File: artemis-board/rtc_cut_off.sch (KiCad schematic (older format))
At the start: 15 parts, among them Q1 2N7002, Q10 AO3401A, Q3 2N7002, U7 PCF8563T, U9 TCA6408A, Y2 32.768KHz

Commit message: added comments and swapped polarity of Vin connector
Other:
- note added: "Optional (if fuel gauge is not available)"
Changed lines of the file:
@@
 	-1   0    0    1
 $EndComp
+Text Notes 5100 3950 0    50   ~ 0
+Optional (if fuel gauge is not available)
+Wire Notes Line
+	5050 2450 5050 3950
+Wire Notes Line
+	5300 2200 6600 2200
 $EndSCHEMATC

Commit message: swapped and added some lcsc part numbers and DNP markers
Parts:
- C22: footprint Capacitor_SMD:C_0603_1608Metric_Pad1.05x0.95mm_HandSolder -> Capacitor_SMD:C_0603_1608Metric_Pad1.08x0.95mm_HandSolder
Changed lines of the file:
@@
 F 0 "C22" H 5600 1700 50  0000 L CNN
 F 1 "1µF" H 5600 1900 50  0000 L CNN
-F 2 "Capacitor_SMD:C_0603_1608Metric_Pad1.05x0.95mm_HandSolder" H 5838 1650 50  0001 C CNN
+F 2 "Capacitor_SMD:C_0603_1608Metric_Pad1.08x0.95mm_HandSolder" H 5838 1650 50  0001 C CNN
 F 3 "~" H 5800 1800 50  0001 C CNN
 F 4 "C15849" H 5800 1800 50  0001 C CNN "LCSC"

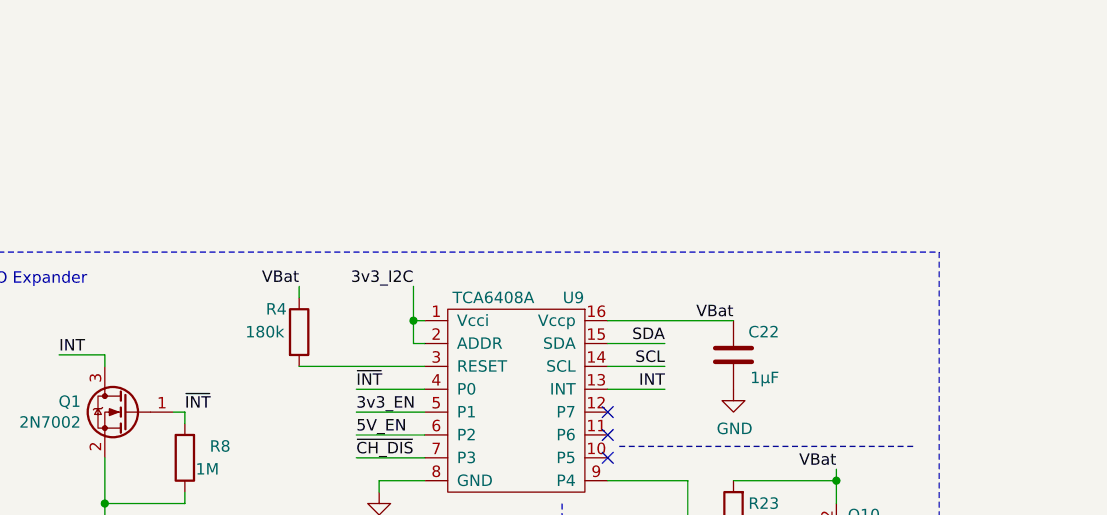
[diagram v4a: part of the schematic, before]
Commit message: added warning comment for expander ic
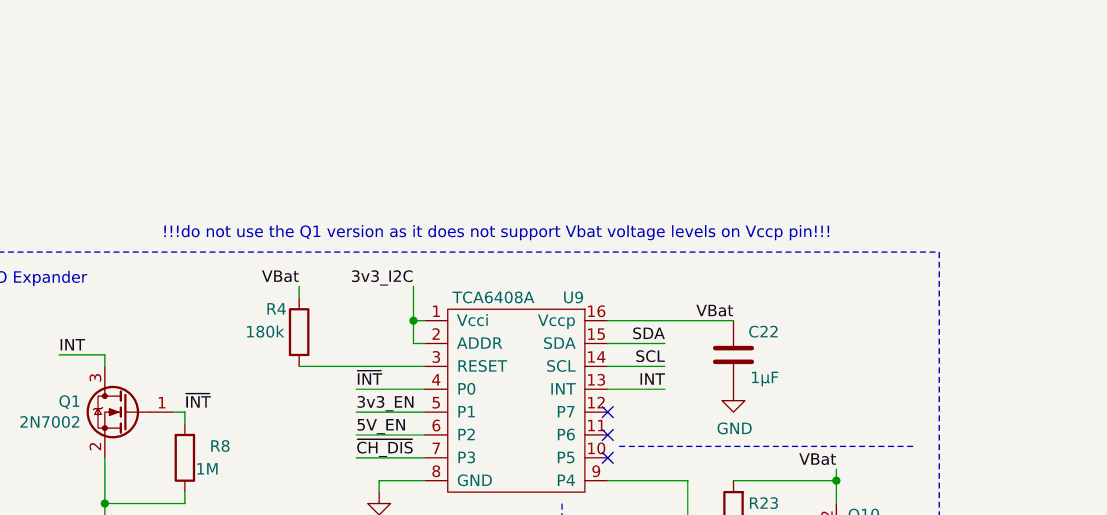
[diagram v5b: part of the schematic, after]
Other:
- note added: "!!!do not use the Q1 version as it does not support Vbat voltage levels on Vccp pin!!!"
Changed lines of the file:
@@
 Wire Notes Line
 	5300 2200 6600 2200
+Text Notes 3300 1300 0    50   ~ 0
+!!!do not use the Q1 version as it does not support Vbat voltage levels on Vccp pin!!!
 $EndSCHEMATC

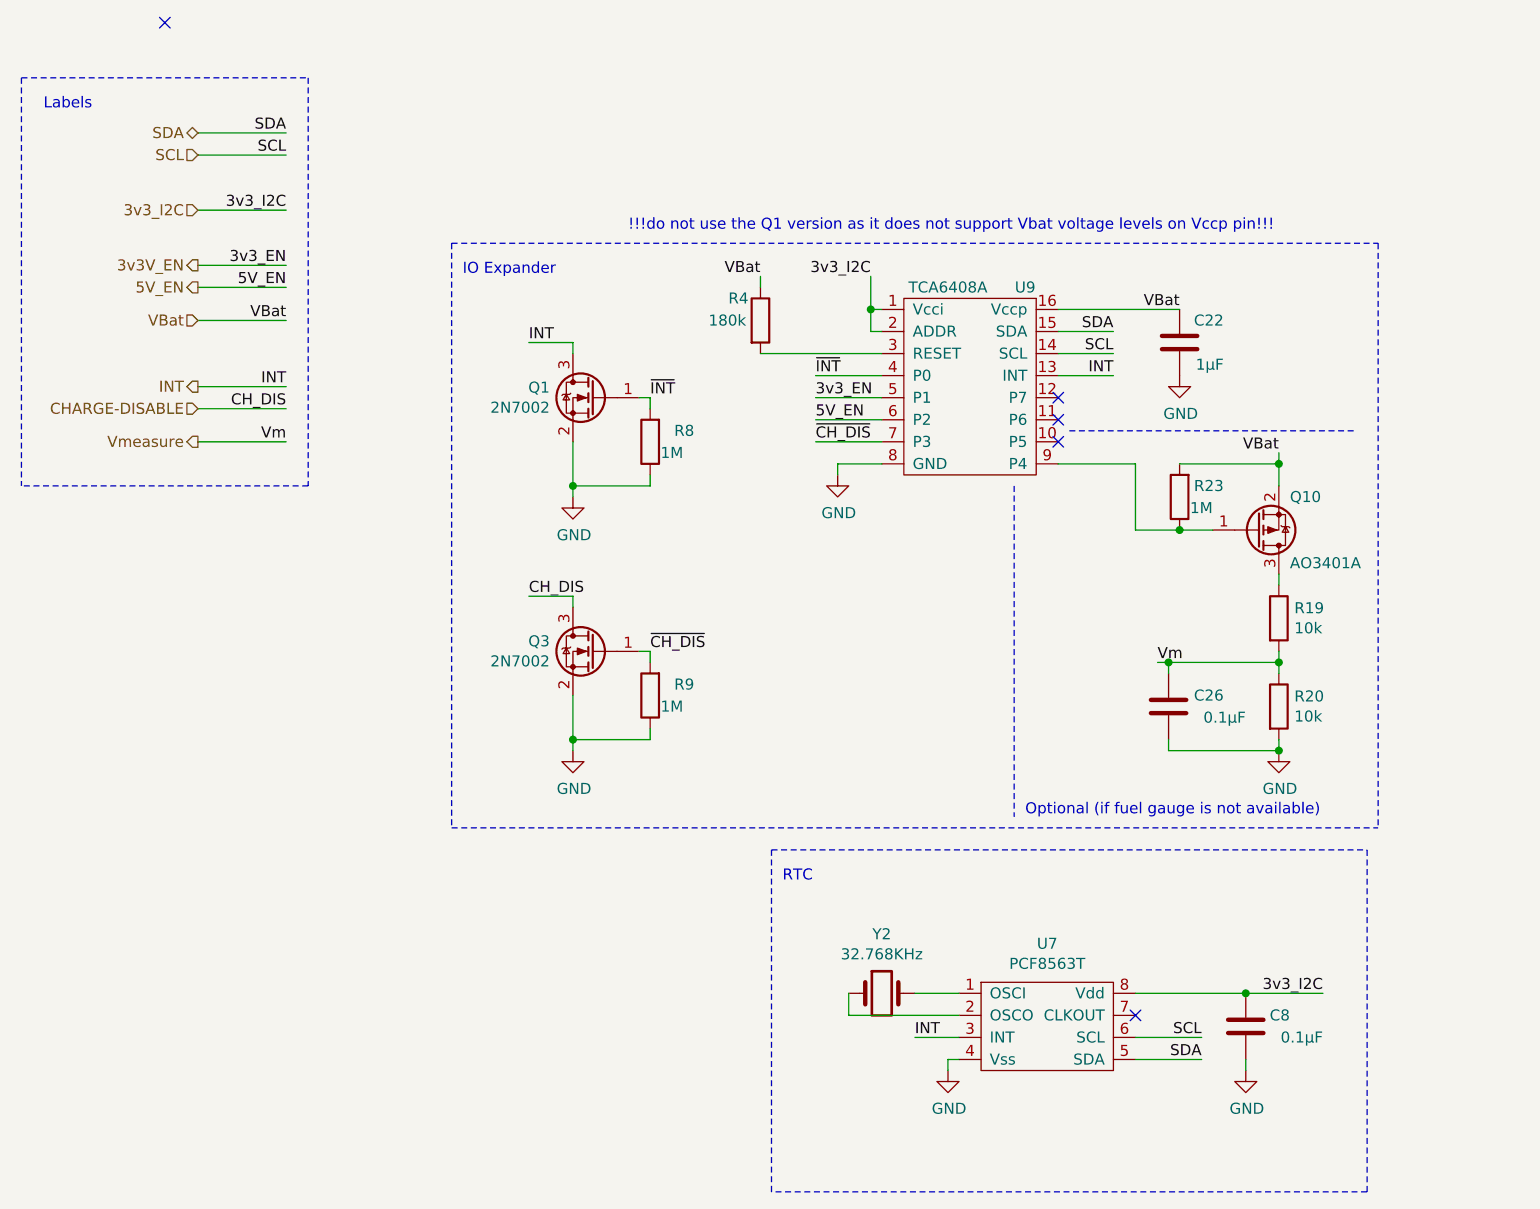
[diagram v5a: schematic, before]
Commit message: connected VccP of io expander back to 3v3, changed some footprint
also added NMos so voltage divider can be used
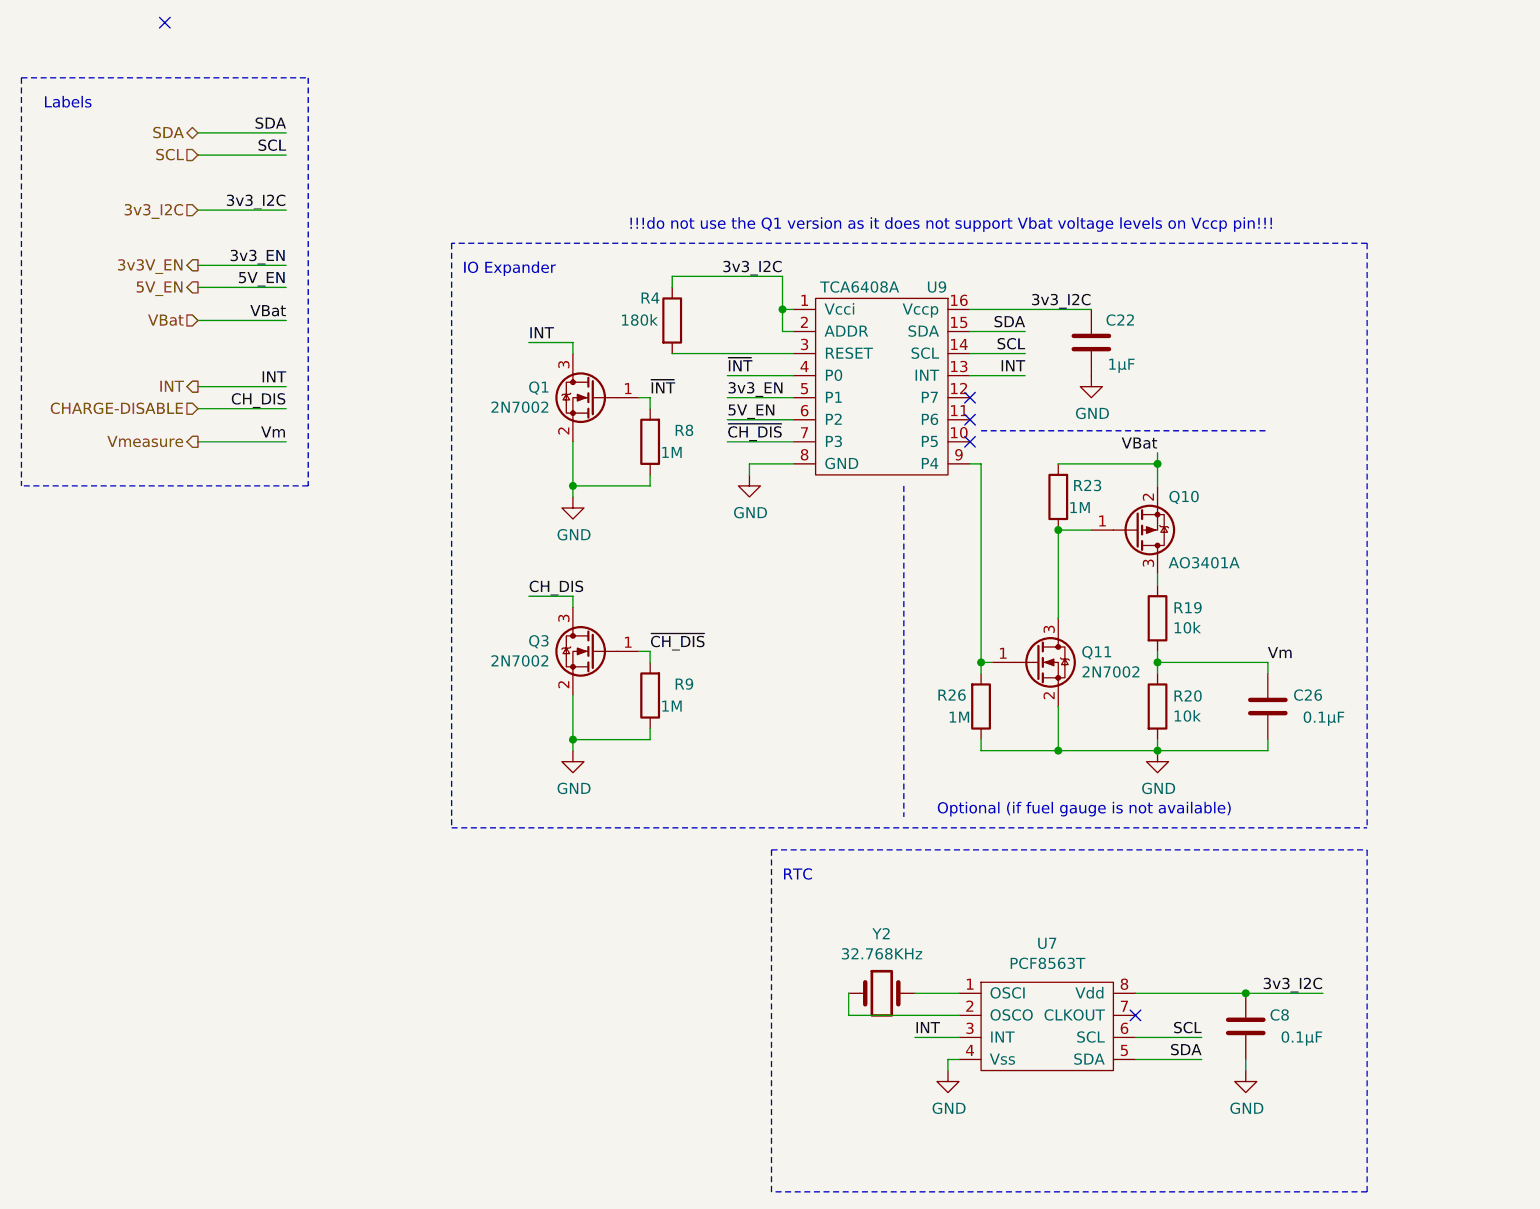
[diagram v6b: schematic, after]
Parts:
- added Q11: 2N7002, Package_TO_SOT_SMD:SOT-23, symbol Transistor_FET:2N7002
- added R26: 1M, Resistor_SMD:R_0603_1608Metric_Pad0.98x0.95mm_HandSolder, symbol Device:R
- Q10: footprint Package_TO_SOT_SMD:SOT-23_Handsoldering -> Package_TO_SOT_SMD:SOT-23
- R23, R8, R9: footprint Resistor_SMD:R_0603_1608Metric_Pad1.05x0.95mm_HandSolder -> Resistor_SMD:R_0603_1608Metric_Pad0.98x0.95mm_HandSolder
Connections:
- net 3v3_I2C: now also C22.2, R4.1, U9.16 (Vccp)
- net GND: now also Q11.2 (S), R26.1
- net VBat: no longer C22.2, R4.1, U9.16 (Vccp)
- net at Q10.1 (G), R23.1: now also Q11.3 (D); no longer U9.9 (P4)
- new net: Q11.1 (G), R26.2, U9.9 (P4)
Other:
- moved on the sheet: C22, C26, Q10, R19, R20, R23, R4, U9

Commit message: added cap to 3v3 I2c, swapped some footprints to normal...
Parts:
- C26, Q10, Q11, R19, R20, R23, R26: DNP (none) -> DNP
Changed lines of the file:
@@
 F 2 "Package_TO_SOT_SMD:SOT-23" H 3350 1975 50  0001 L CIN
 F 3 "https://www.fairchildsemi.com/datasheets/2N/2N7002.pdf" H 3150 2050 50  0001 L CNN
-F 4 "" H 3150 2050 50  0001 C CNN "Field4"
-F 5 "C8545" H 3150 2050 50  0001 C CNN "LCSC"
+F 4 "C8545" H 3150 2050 50  0001 C CNN "LCSC"
 	1    3150 2050
 	-1   0    0    -1
@@
 F 2 "Package_TO_SOT_SMD:SOT-23" H 3350 3125 50  0001 L CIN
 F 3 "https://www.fairchildsemi.com/datasheets/2N/2N7002.pdf" H 3150 3200 50  0001 L CNN
-F 4 "" H 3150 3200 50  0001 C CNN "Field4"
-F 5 "C8545" H 3150 3200 50  0001 C CNN "LCSC"
+F 4 "C8545" H 3150 3200 50  0001 C CNN "LCSC"
 	1    3150 3200
 	-1   0    0    -1
@@
 F 3 "~" H 4900 3450 50  0001 C CNN
 F 4 "C22935" H 4900 3450 50  0001 C CNN "LCSC"
+F 5 "DNP" H 4900 3450 50  0001 C CNN "DNP"
 	1    4900 3450
 	1    0    0    1
@@
 F 2 "Package_TO_SOT_SMD:SOT-23" H 5350 3175 50  0001 L CIN
 F 3 "https://www.fairchildsemi.com/datasheets/2N/2N7002.pdf" H 5150 3250 50  0001 L CNN
-F 4 "" H 5150 3250 50  0001 C CNN "Field4"
-F 5 "C8545" H 5150 3250 50  0001 C CNN "LCSC"
+F 4 "C8545" H 5150 3250 50  0001 C CNN "LCSC"
+F 5 "DNP" H 5150 3250 50  0001 C CNN "DNP"
 	1    5150 3250
 	1    0    0    -1
@@
 F 3 "~" H 6200 3450 50  0001 C CNN
 F 4 "C14858" H 6200 3450 50  0001 C CNN "LCSC"
+F 5 "DNP" H 6200 3450 50  0001 C CNN "DNP"
 	1    6200 3450
 	-1   0    0    1
@@
 F 3 "~" H 5250 2500 50  0001 C CNN
 F 4 "C22935" H 5250 2500 50  0001 C CNN "LCSC"
+F 5 "DNP" H 5250 2500 50  0001 C CNN "DNP"
 	1    5250 2500
 	-1   0    0    1
@@
 F 3 "http://www.aosmd.com/pdfs/datasheet/AO3401A.pdf" H 5600 2650 50  0001 L CNN
 F 4 "C15127" H 5600 2650 50  0001 C CNN "LCSC"
+F 5 "DNP" H 5600 2650 50  0001 C CNN "DNP"
 	1    5600 2650
 	1    0    0    1
@@
 F 3 "~" H 5700 3450 50  0001 C CNN
 F 4 "C25804" H 5700 3450 50  0001 C CNN "LCSC"
+F 5 "DNP" H 5700 3450 50  0001 C CNN "DNP"
 	1    5700 3450
 	1    0    0    -1
@@
 F 3 "~" H 5700 3050 50  0001 C CNN
 F 4 "C25804" H 5700 3050 50  0001 C CNN "LCSC"
+F 5 "DNP" H 5700 3050 50  0001 C CNN "DNP"
 	1    5700 3050
 	1    0    0    -1

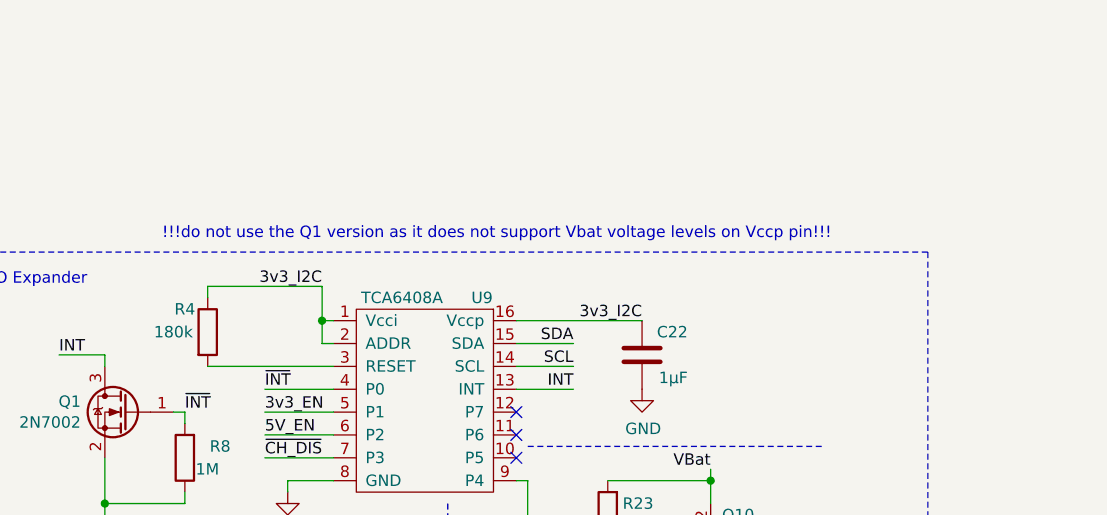
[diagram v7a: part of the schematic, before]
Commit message: removed voltage level warning for io expander due to Vccp on 3v3
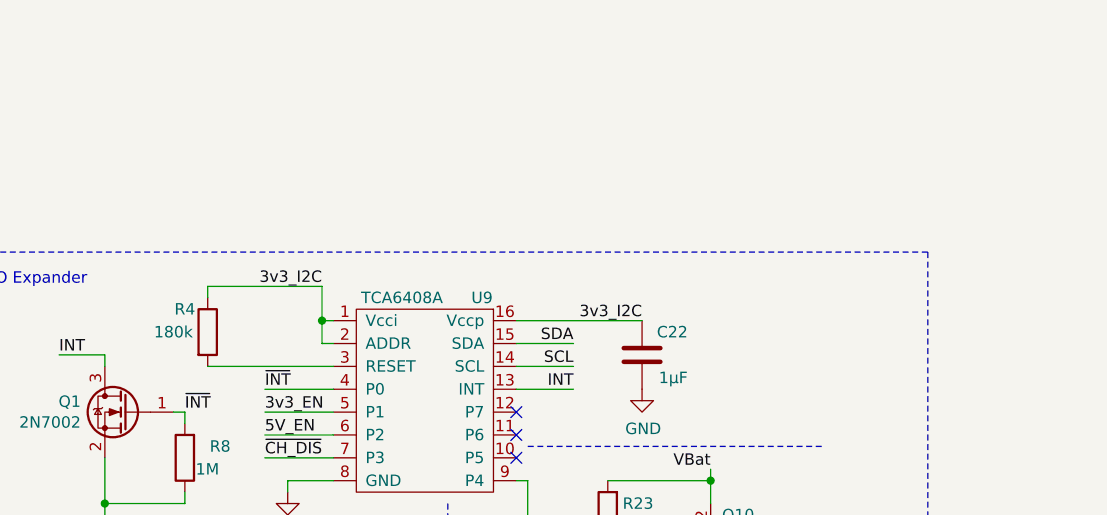
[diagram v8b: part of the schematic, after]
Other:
- note removed: "!!!do not use the Q1 version as it does not support Vbat voltage levels on Vccp pin!!!"
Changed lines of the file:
@@
 Wire Notes Line
 	4900 2200 6200 2200
-Text Notes 3300 1300 0    50   ~ 0
-!!!do not use the Q1 version as it does not support Vbat voltage levels on Vccp pin!!!
 Connection ~ 5700 2350
 Wire Wire Line
